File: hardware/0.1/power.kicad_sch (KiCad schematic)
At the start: 59 parts, among them U301 CYUSB3014-BZXx, U701 TLV62569DRLR, U703 TLV62569DRLR, U704 TLV62569DRLR

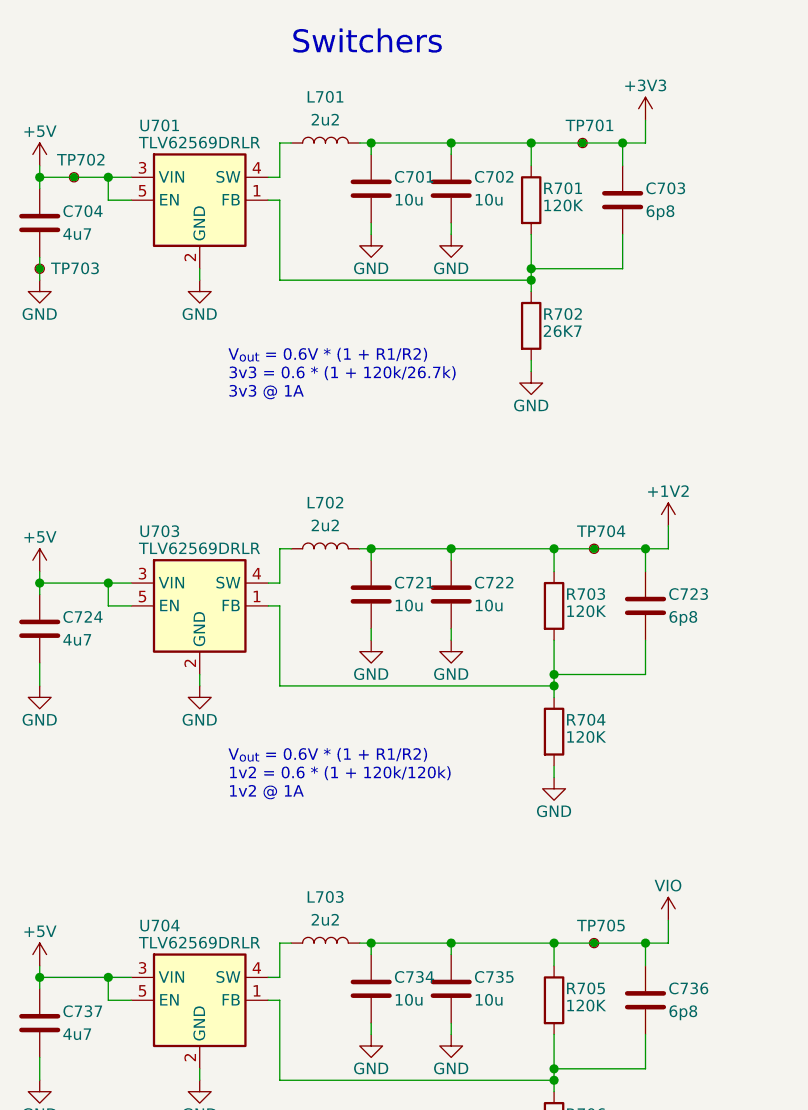
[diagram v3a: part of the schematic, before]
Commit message: usb3 routed less tuning
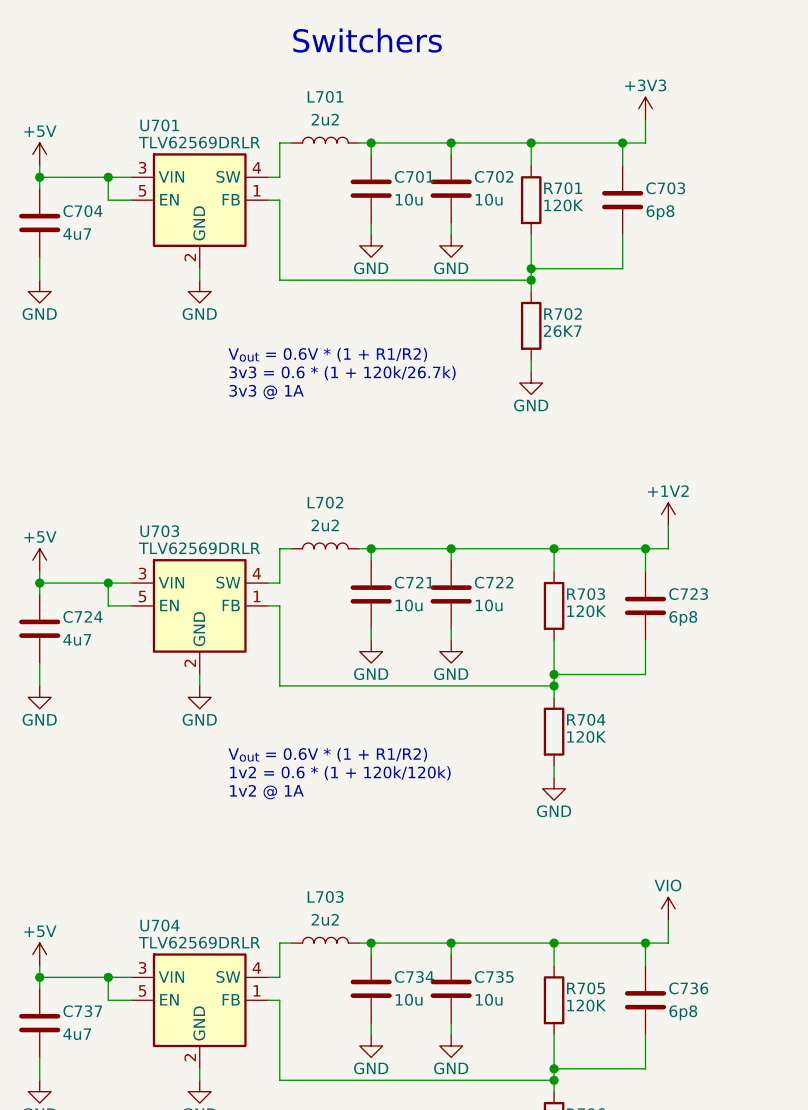
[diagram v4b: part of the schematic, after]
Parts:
- removed TP701, TP702, TP704, TP705: TP, josh-test-point:TestPoint_SMDPad_D0.5mm_NO_SILK, symbol Connector:TestPoint_Small
- removed TP703: TP, josh-test-point:S1751-46_smdTestPoint, symbol Connector:TestPoint_Small
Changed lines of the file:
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@@
   (junction (at 191.135 142.875) (diameter 0) (color 0 0 0 0)
   )
-  (junction (at 31.115 36.83) (diameter 0) (color 0 0 0 0)
-  )
   (junction (at 227.33 118.745) (diameter 0) (color 0 0 0 0)
   )
@@
   (junction (at 172.085 109.855) (diameter 0) (color 0 0 0 0)
   )
-  (junction (at 87.63 33.02) (diameter 0) (color 0 0 0 0)
-  )
   (junction (at 224.79 52.705) (diameter 0) (color 0 0 0 0)
   )
@@
   (junction (at 190.5 52.705) (diameter 0) (color 0 0 0 0)
   )
-  (junction (at 88.9 78.105) (diameter 0) (color 0 0 0 0)
-  )
   (junction (at 84.455 93.345) (diameter 1.016) (color 0 0 0 0)
   )
@@
   (junction (at 225.425 145.415) (diameter 0) (color 0 0 0 0)
   )
-  (junction (at 88.9 121.92) (diameter 0) (color 0 0 0 0)
-  )
   (junction (at 190.5 55.245) (diameter 0) (color 0 0 0 0)
   )
@@
   )
   (junction (at 147.955 55.88) (diameter 0) (color 0 0 0 0)
-  )
-  (junction (at 27.305 46.99) (diameter 0) (color 0 0 0 0)
   )
   (junction (at 128.27 55.88) (diameter 0) (color 0 0 0 0)
@@
     (stroke (width 0) (type solid) (color 0 0 0 0))
   )
-  (wire (pts (xy 81.915 33.02) (xy 87.63 33.02))
+  (wire (pts (xy 81.915 33.02) (xy 92.075 33.02))
     (stroke (width 0) (type solid) (color 0 0 0 0))
   )
@@
     (stroke (width 0) (type solid) (color 0 0 0 0))
   )
-  (wire (pts (xy 87.63 33.02) (xy 92.075 33.02))
-    (stroke (width 0) (type solid) (color 0 0 0 0))
-  )
   (wire (pts (xy 27.305 134.62) (xy 27.305 137.16))
     (stroke (width 0) (type solid) (color 0 0 0 0))
@@
     (stroke (width 0) (type default) (color 0 0 0 0))
   )
+  (wire (pts (xy 27.305 45.72) (xy 27.305 48.26))
+    (stroke (width 0) (type default) (color 0 0 0 0))
+  )
   (wire (pts (xy 97.155 121.92) (xy 97.155 119.38))
     (stroke (width 0) (type solid) (color 0 0 0 0))
@@
     (stroke (width 0) (type solid) (color 0 0 0 0))
   )
-  (wire (pts (xy 27.305 46.99) (xy 27.305 48.26))
-    (stroke (width 0) (type solid) (color 0 0 0 0))
-  )
   (wire (pts (xy 191.135 117.475) (xy 191.135 120.015))
     (stroke (width 0) (type default) (color 0 0 0 0))
@@
     (stroke (width 0) (type solid) (color 0 0 0 0))
   )
-  (wire (pts (xy 84.455 121.92) (xy 88.9 121.92))
-    (stroke (width 0) (type solid) (color 0 0 0 0))
-  )
   (wire (pts (xy 193.04 79.375) (xy 189.865 79.375))
     (stroke (width 0) (type default) (color 0 0 0 0))
   )
-  (wire (pts (xy 31.115 36.83) (xy 27.305 36.83))
+  (wire (pts (xy 27.305 36.83) (xy 34.925 36.83))
     (stroke (width 0) (type solid) (color 0 0 0 0))
   )
@@
     (stroke (width 0) (type default) (color 0 0 0 0))
   )
-  (wire (pts (xy 84.455 78.105) (xy 88.9 78.105))
+  (wire (pts (xy 84.455 78.105) (xy 94.615 78.105))
     (stroke (width 0) (type solid) (color 0 0 0 0))
   )
@@
     (stroke (width 0) (type solid) (color 0 0 0 0))
   )
-  (wire (pts (xy 88.9 121.92) (xy 94.615 121.92))
+  (wire (pts (xy 84.455 121.92) (xy 94.615 121.92))
     (stroke (width 0) (type solid) (color 0 0 0 0))
   )
@@
     (stroke (width 0) (type solid) (color 0 0 0 0))
   )
-  (wire (pts (xy 88.9 78.105) (xy 94.615 78.105))
-    (stroke (width 0) (type solid) (color 0 0 0 0))
-  )
   (wire (pts (xy 244.475 76.2) (xy 244.475 76.835))
     (stroke (width 0) (type default) (color 0 0 0 0))
@@
     (stroke (width 0) (type default) (color 0 0 0 0))
   )
-  (wire (pts (xy 34.925 36.83) (xy 31.115 36.83))
-    (stroke (width 0) (type solid) (color 0 0 0 0))
-  )
   (wire (pts (xy 163.195 109.855) (xy 163.195 110.49))
     (stroke (width 0) (type default) (color 0 0 0 0))
@@
   (wire (pts (xy 246.38 92.075) (xy 246.38 93.345))
     (stroke (width 0) (type default) (color 0 0 0 0))
-  )
-  (wire (pts (xy 27.305 45.72) (xy 27.305 46.99))
-    (stroke (width 0) (type solid) (color 0 0 0 0))
   )
   (wire (pts (xy 73.025 78.105) (xy 84.455 78.105))
@@
     )
     (property "Datasheet" "" (id 3) (at 27.305 93.345 0)
-      (effects (font (size 1.27 1.27)) hide)
-    )
-    (pin "1")
-  )
-  (symbol (lib_id "Connector:TestPoint_Small") (at 31.115 36.83 0) (unit 1)
-    (in_bom no) (on_board yes)
-    (property "Reference" "TP702" (id 0) (at 29.2359 34.925 0)
-      (effects (font (size 1.27 1.27)) (justify left))
-    )
-    (property "Value" "TP" (id 1) (at 32.385 38.0999 0)
-      (effects (font (size 1.27 1.27)) (justify left) hide)
-    )
-    (property "Footprint" "josh-test-point:TestPoint_SMDPad_D0.5mm_NO_SILK" (id 2) (at 36.195 36.83 0)
-      (effects (font (size 1.27 1.27)) hide)
-    )
-    (property "Datasheet" "~" (id 3) (at 36.195 36.83 0)
       (effects (font (size 1.27 1.27)) hide)
     )
@@
     (pin "1")
   )
-  (symbol (lib_id "Connector:TestPoint_Small") (at 88.9 121.92 0) (unit 1)
-    (in_bom no) (on_board yes)
-    (property "Reference" "TP705" (id 0) (at 87.0209 120.015 0)
-      (effects (font (size 1.27 1.27)) (justify left))
-    )
-    (property "Value" "TP" (id 1) (at 90.17 123.1899 0)
-      (effects (font (size 1.27 1.27)) (justify left) hide)
-    )
-    (property "Footprint" "josh-test-point:TestPoint_SMDPad_D0.5mm_NO_SILK" (id 2) (at 93.98 121.92 0)
-      (effects (font (size 1.27 1.27)) hide)
-    )
-    (property "Datasheet" "~" (id 3) (at 93.98 121.92 0)
-      (effects (font (size 1.27 1.27)) hide)
-    )
-    (pin "1")
-  )
   (symbol (lib_id "Device:R") (at 81.915 53.34 0) (unit 1)
     (in_bom yes) (on_board yes)
@@
     (pin "2")
   )
-  (symbol (lib_id "Connector:TestPoint_Small") (at 87.63 33.02 0) (unit 1)
-    (in_bom no) (on_board yes)
-    (property "Reference" "TP701" (id 0) (at 85.7509 31.115 0)
-      (effects (font (size 1.27 1.27)) (justify left))
-    )
-    (property "Value" "TP" (id 1) (at 88.9 34.2899 0)
-      (effects (font (size 1.27 1.27)) (justify left) hide)
-    )
-    (property "Footprint" "josh-test-point:TestPoint_SMDPad_D0.5mm_NO_SILK" (id 2) (at 92.71 33.02 0)
-      (effects (font (size 1.27 1.27)) hide)
-    )
-    (property "Datasheet" "~" (id 3) (at 92.71 33.02 0)
-      (effects (font (size 1.27 1.27)) hide)
-    )
-    (pin "1")
-  )
-  (symbol (lib_id "Connector:TestPoint_Small") (at 88.9 78.105 0) (unit 1)
-    (in_bom no) (on_board yes)
-    (property "Reference" "TP704" (id 0) (at 87.0209 76.2 0)
-      (effects (font (size 1.27 1.27)) (justify left))
-    )
-    (property "Value" "TP" (id 1) (at 90.17 79.3749 0)
-      (effects (font (size 1.27 1.27)) (justify left) hide)
-    )
-    (property "Footprint" "josh-test-point:TestPoint_SMDPad_D0.5mm_NO_SILK" (id 2) (at 93.98 78.105 0)
-      (effects (font (size 1.27 1.27)) hide)
-    )
-    (property "Datasheet" "~" (id 3) (at 93.98 78.105 0)
-      (effects (font (size 1.27 1.27)) hide)
-    )
-    (pin "1")
-  )
-  (symbol (lib_id "Connector:TestPoint_Small") (at 27.305 46.99 0) (unit 1)
-    (in_bom yes) (on_board yes)
-    (property "Reference" "TP703" (id 0) (at 28.575 46.99 0)
-      (effects (font (size 1.27 1.27)) (justify left))
-    )
-    (property "Value" "TP" (id 1) (at 28.575 48.2599 0)
-      (effects (font (size 1.27 1.27)) (justify left) hide)
-    )
-    (property "Footprint" "josh-test-point:S1751-46_smdTestPoint" (id 2) (at 32.385 46.99 0)
-      (effects (font (size 1.27 1.27)) hide)
-    )
-    (property "Datasheet" "~" (id 3) (at 32.385 46.99 0)
-      (effects (font (size 1.27 1.27)) hide)
-    )
-    (property "Digikey" "952-3024-ND" (id 4) (at 27.305 46.99 0)
-      (effects (font (size 1.27 1.27)) hide)
-    )
-    (property "MPN" "S1751-46 " (id 5) (at 27.305 46.99 0)
-      (effects (font (size 1.27 1.27)) hide)
-    )
-    (property "Manufacturer" "Harwin" (id 6) (at 27.305 46.99 0)
-      (effects (font (size 1.27 1.27)) hide)
-    )
-    (pin "1")
-  )
   (symbol (lib_id "power:GND") (at 236.855 62.23 0) (unit 1)

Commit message: component shortage changes
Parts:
- C703, C723, C736: LCSC C1525 -> C88896; MPN CL05B104KO5NNNC -> GJM1555C1H6R8BB01D; Manufacturer Samsung Electro-Mechanics -> Murata Electronics
- L701, L702, L703: Digikey (none) -> 490-7781-2-ND
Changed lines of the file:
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@@
       (effects (font (size 1.27 1.27)) hide)
     )
-    (property "LCSC" "C1525" (id 4) (at 94.615 84.455 0)
-      (effects (font (size 1.27 1.27)) hide)
-    )
-    (property "MPN" "CL05B104KO5NNNC" (id 5) (at 94.615 84.455 0)
-      (effects (font (size 1.27 1.27)) hide)
-    )
-    (property "Manufacturer" "Samsung Electro-Mechanics" (id 6) (at 94.615 84.455 0)
+    (property "LCSC" "C88896" (id 4) (at 94.615 84.455 0)
+      (effects (font (size 1.27 1.27)) hide)
+    )
+    (property "MPN" "GJM1555C1H6R8BB01D" (id 5) (at 94.615 84.455 0)
+      (effects (font (size 1.27 1.27)) hide)
+    )
+    (property "Manufacturer" "Murata Electronics" (id 6) (at 94.615 84.455 0)
       (effects (font (size 1.27 1.27)) hide)
     )
@@
       (effects (font (size 1.27 1.27)) hide)
     )
-    (property "LCSC" "C1525" (id 4) (at 94.615 128.27 0)
-      (effects (font (size 1.27 1.27)) hide)
-    )
-    (property "MPN" "CL05B104KO5NNNC" (id 5) (at 94.615 128.27 0)
-      (effects (font (size 1.27 1.27)) hide)
-    )
-    (property "Manufacturer" "Samsung Electro-Mechanics" (id 6) (at 94.615 128.27 0)
+    (property "LCSC" "C88896" (id 4) (at 94.615 128.27 0)
+      (effects (font (size 1.27 1.27)) hide)
+    )
+    (property "MPN" "GJM1555C1H6R8BB01D" (id 5) (at 94.615 128.27 0)
+      (effects (font (size 1.27 1.27)) hide)
+    )
+    (property "Manufacturer" "Murata Electronics" (id 6) (at 94.615 128.27 0)
       (effects (font (size 1.27 1.27)) hide)
     )
@@
       (effects (font (size 1.27 1.27)) hide)
     )
-    (property "LCSC" "C1525" (id 4) (at 92.075 39.37 0)
-      (effects (font (size 1.27 1.27)) hide)
-    )
-    (property "MPN" "CL05B104KO5NNNC" (id 5) (at 92.075 39.37 0)
-      (effects (font (size 1.27 1.27)) hide)
-    )
-    (property "Manufacturer" "Samsung Electro-Mechanics" (id 6) (at 92.075 39.37 0)
+    (property "LCSC" "C88896" (id 4) (at 92.075 39.37 0)
+      (effects (font (size 1.27 1.27)) hide)
+    )
+    (property "MPN" "GJM1555C1H6R8BB01D" (id 5) (at 92.075 39.37 0)
+      (effects (font (size 1.27 1.27)) hide)
+    )
+    (property "Manufacturer" "Murata Electronics" (id 6) (at 92.075 39.37 0)
       (effects (font (size 1.27 1.27)) hide)
     )
@@
       (effects (font (size 1.27 1.27)) hide)
     )
+    (property "Digikey" "490-7781-2-ND" (id 9) (at 59.055 78.105 0)
+      (effects (font (size 1.27 1.27)) hide)
+    )
     (pin "1")
     (pin "2")
@@
       (effects (font (size 1.27 1.27)) hide)
     )
+    (property "Digikey" "490-7781-2-ND" (id 9) (at 59.055 121.92 0)
+      (effects (font (size 1.27 1.27)) hide)
+    )
     (pin "1")
     (pin "2")
@@
       (effects (font (size 1.27 1.27)) hide)
     )
+    (property "Digikey" "490-7781-2-ND" (id 9) (at 59.055 33.02 0)
+      (effects (font (size 1.27 1.27)) hide)
+    )
